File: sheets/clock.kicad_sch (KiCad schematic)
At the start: 27 parts, among them U33 74HC04, U39 CX23065A, U8 74HC04, X1 24.167829MHz, X2 3.579545MHz

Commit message: Merged in schematics from stable with footprints
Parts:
- D3: footprint (none) -> Diode_THT:D_A-405_P10.16mm_Horizontal
- TP1, TP2: footprint (none) -> TestPoint:TestPoint_Pad_D4.0mm
- U33, U8: footprint (none) -> Package_DIP:DIP-14_W7.62mm
- X1, X2: footprint (none) -> Crystal:Crystal_HC33-U_Horizontal

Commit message: FIX 74AS04 and 74HC04
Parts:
- removed unit 4 of U8
- added unit 5 of U8
- renumbered U33 to U8, U8 to U80
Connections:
- net DIVI: now also U8.10; no longer U8.12
- net at C55.2, R72.1, TC1.1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: now also U8.13
- net at C52.2, C65.1, R72.2: now also U8.12, U8.11; no longer U8.13
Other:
- moved on the sheet: U8F

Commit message: Forgot Footprint on U8
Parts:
- U8: footprint (none) -> Package_DIP:DIP-14_W7.62mm
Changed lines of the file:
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@@
     (property "Reference" "U8" (id 0) (at 311.912 110.49 0))
     (property "Value" "74HC04" (id 1) (at 313.436 119.888 0))
-    (property "Footprint" "" (id 2) (at 312.166 115.316 0)
+    (property "Footprint" "Package_DIP:DIP-14_W7.62mm" (id 2) (at 312.166 115.316 0)
       (effects (font (size 1.27 1.27)) hide)
     )

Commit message: Sync footprints from Nightly Build
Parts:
- U39: footprint Package_DIP:DIP-28_W15.24mm -> 1_NeoGeoLibrary:CX23065A
- X1, X2: footprint Crystal:Crystal_HC33-U_Horizontal -> 1_NeoGeoLibrary:Crystal
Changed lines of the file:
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@@
     (property "Reference" "X1" (id 0) (at 139.7 97.155 0))
     (property "Value" "24.167829MHz" (id 1) (at 146.685 105.41 0))
-    (property "Footprint" "Crystal:Crystal_HC33-U_Horizontal" (id 2) (at 139.7 100.965 0)
+    (property "Footprint" "1_NeoGeoLibrary:Crystal" (id 2) (at 139.7 100.965 0)
       (effects (font (size 1.27 1.27)) hide)
     )
@@
     (property "Reference" "U39" (id 0) (at 189.23 147.955 0))
     (property "Value" "CX23065A" (id 1) (at 194.945 166.37 0))
-    (property "Footprint" "Package_DIP:DIP-28_W15.24mm" (id 2) (at 194.945 174.625 0)
+    (property "Footprint" "1_NeoGeoLibrary:CX23065A" (id 2) (at 194.945 174.625 0)
       (effects (font (size 1.27 1.27)) hide)
     )
@@
     (property "Reference" "X2" (id 0) (at 261.366 81.661 0))
     (property "Value" "3.579545MHz" (id 1) (at 266.446 89.281 0))
-    (property "Footprint" "Crystal:Crystal_HC33-U_Horizontal" (id 2) (at 261.366 85.471 0)
+    (property "Footprint" "1_NeoGeoLibrary:Crystal" (id 2) (at 261.366 85.471 0)
       (effects (font (size 1.27 1.27)) hide)
     )

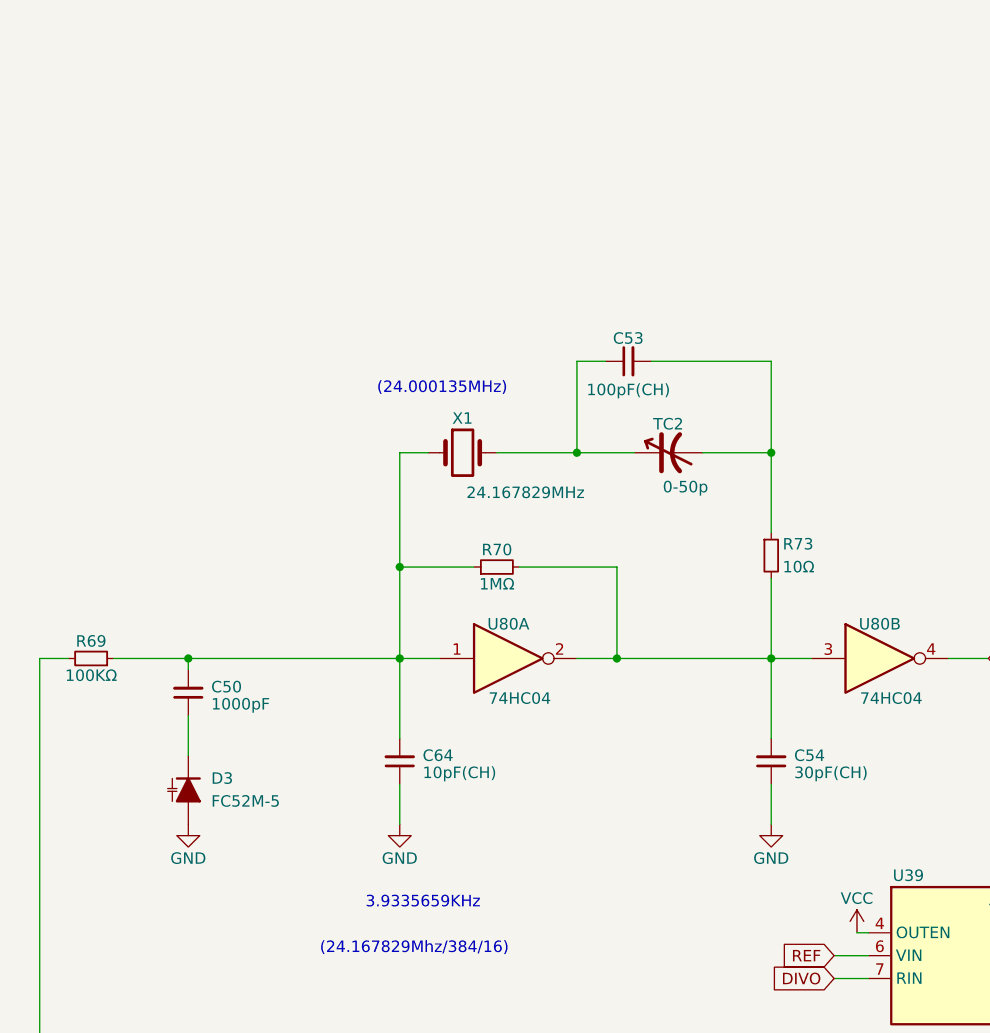
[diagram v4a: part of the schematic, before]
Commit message: Redo Video Clock Signal (1)
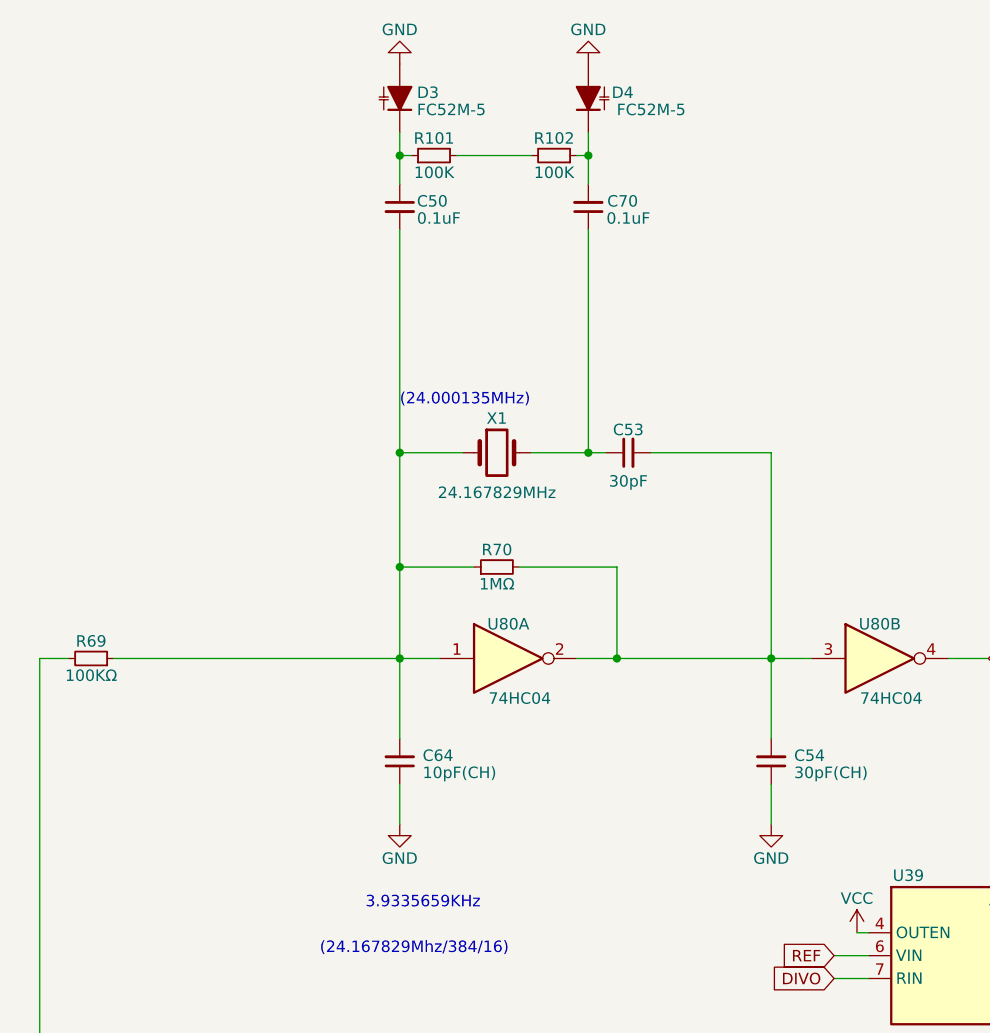
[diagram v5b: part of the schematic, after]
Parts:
- removed R73: 10Ω, 1_NeoGeoLibrary:Resistor1-5mm, symbol Device:R_Small
- removed TC2: 0-50p, Resistor_THT:R_Axial_DIN0204_L3.6mm_D1.6mm_P5.08mm_Vertical, symbol Device:C_Variable
- added C70: 0.1uF, 1_NeoGeoLibrary:CAP1-5mm, symbol Device:C_Small
- added D4: FC52M-5, Package_TO_SOT_THT:SOD-70_P2.54mm, symbol Device:D_Capacitance_Filled
- added R101, R102: 100K, 1_NeoGeoLibrary:Resistor1-5mm, symbol Device:R_Small
- C50: value 1000pF -> 0.1uF
- C53: value 100pF(CH) -> 30pF
- D3: footprint Diode_THT:D_A-405_P10.16mm_Horizontal -> Package_TO_SOT_THT:SOD-70_P2.54mm
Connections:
- net GND: now also D4.2 (A)
- net at C53.2: now also C54.2, R70.2, U80.2, U80.3
- net at C53.1, X1.2: now also C70.1
- net at C50.1, D3.1 (K): now also R101.1
- new net: R101.2, R102.2
- new net: C70.2, D4.1 (K), R102.1
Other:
- moved on the sheet: C50, C53, D3, X1

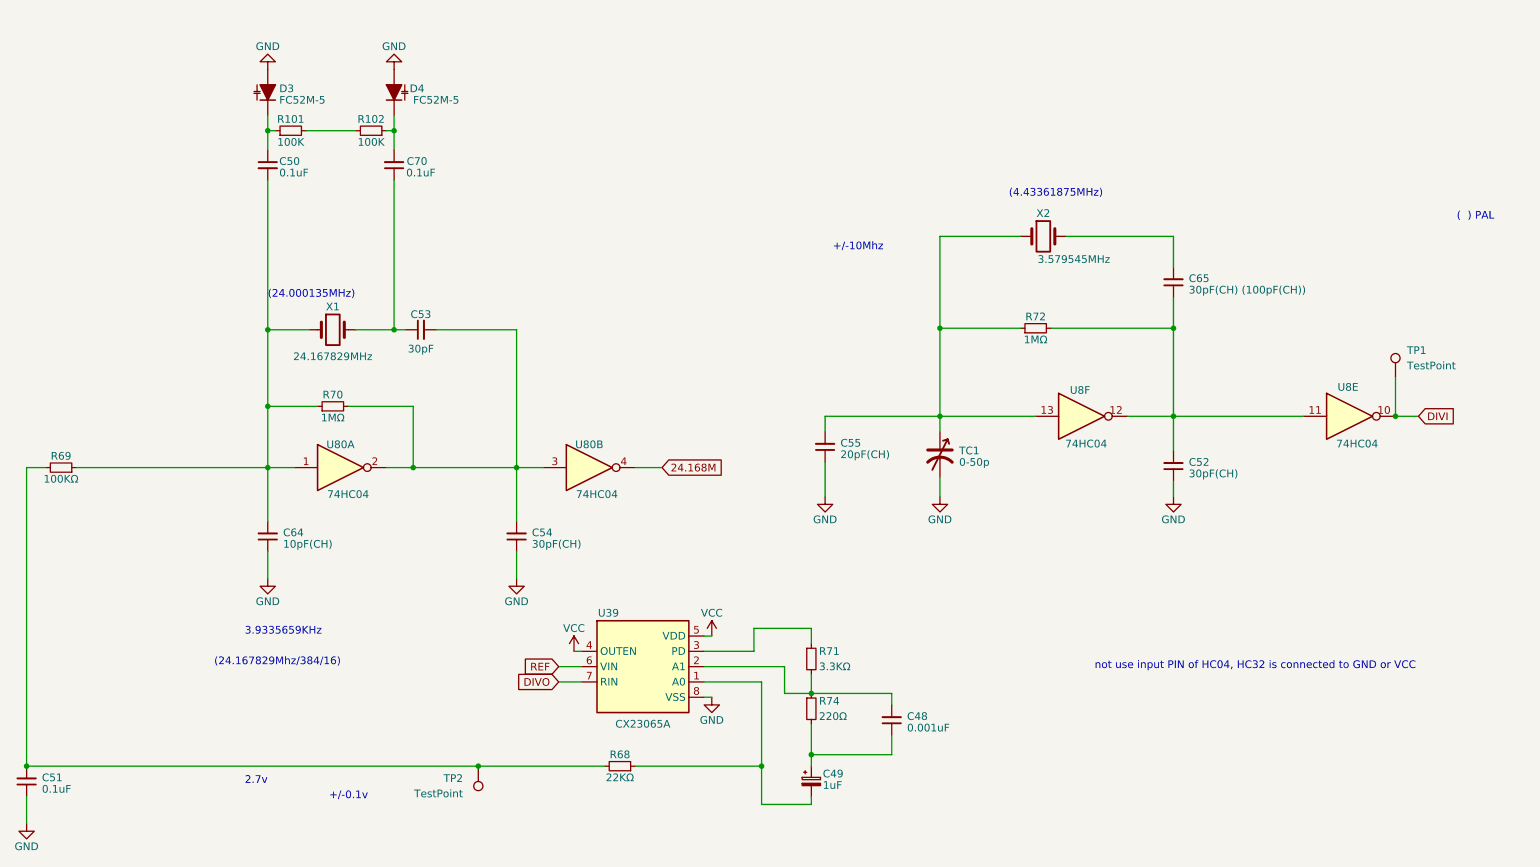
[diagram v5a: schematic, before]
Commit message: Redo Video Clock Signal (2)
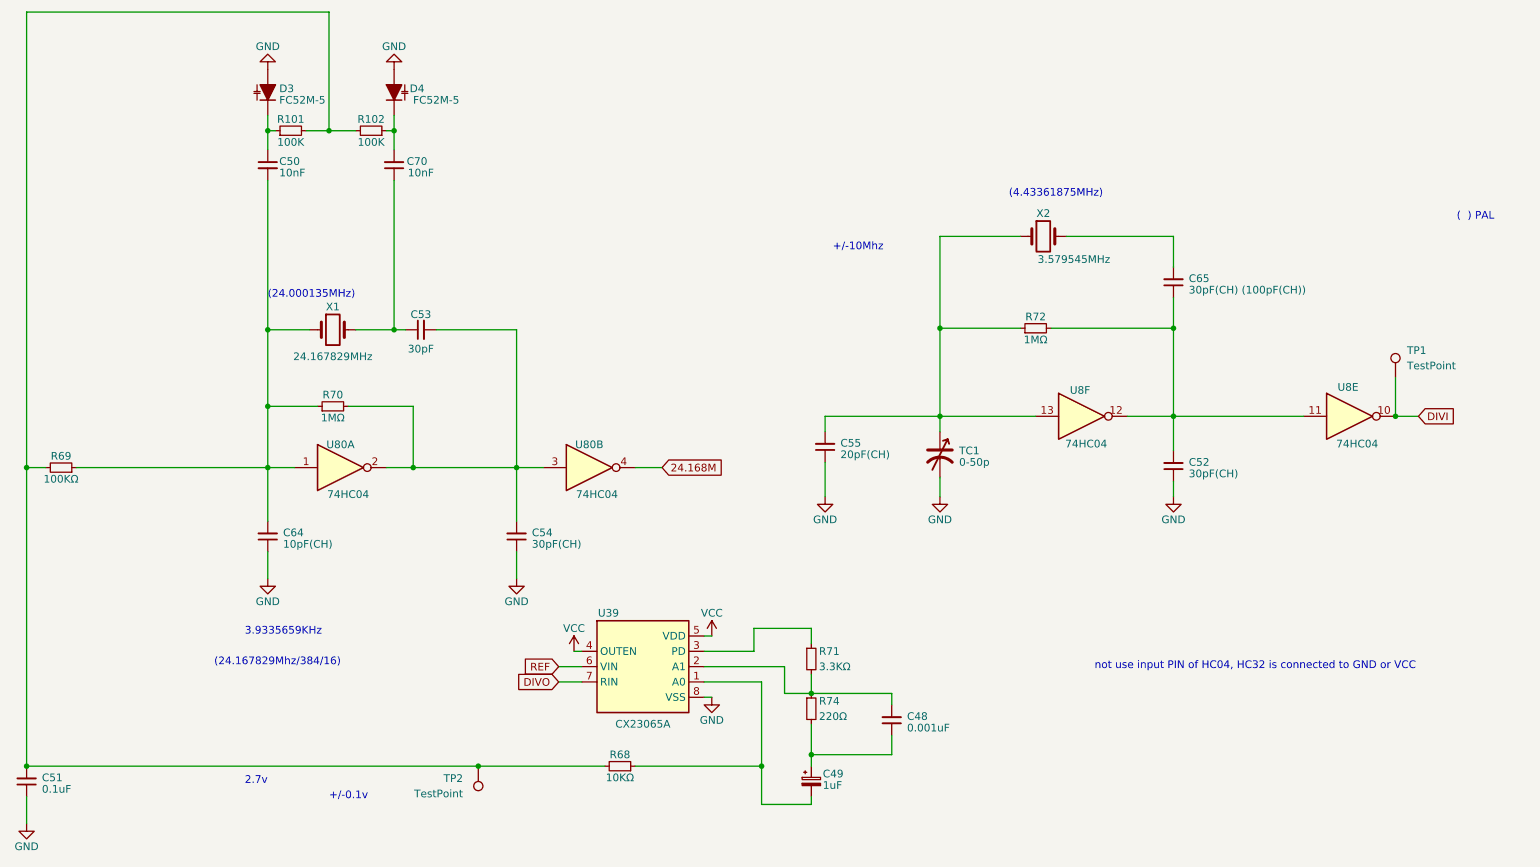
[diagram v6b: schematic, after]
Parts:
- C50, C70: value 0.1uF -> 10nF; footprint 1_NeoGeoLibrary:CAP1-5mm -> 1_NeoGeoLibrary:CAP3-5mm
- R68: value 22KΩ -> 10KΩ
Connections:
- net at C51.2, R68.2, R69.2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: now also R101.2, R102.2
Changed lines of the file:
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@@
   (junction (at 319.786 115.316) (diameter 0) (color 0 0 0 0)
   )
+  (junction (at 142.875 67.945) (diameter 0) (color 0 0 0 0)
+  )
+  (junction (at 92.71 123.825) (diameter 0) (color 0 0 0 0)
+  )
   (junction (at 132.715 100.965) (diameter 0) (color 0 0 0 0)
   )
@@
     (stroke (width 0) (type default) (color 0 0 0 0))
   )
+  (wire (pts (xy 92.71 48.26) (xy 92.71 123.825))
+    (stroke (width 0) (type default) (color 0 0 0 0))
+  )
   (wire (pts (xy 132.715 65.405) (xy 132.715 67.945))
     (stroke (width 0) (type default) (color 0 0 0 0))
@@
     (stroke (width 0) (type default) (color 0 0 0 0))
   )
-  (wire (pts (xy 139.065 67.945) (xy 147.32 67.945))
+  (wire (pts (xy 139.065 67.945) (xy 142.875 67.945))
     (stroke (width 0) (type default) (color 0 0 0 0))
   )
@@
     (stroke (width 0) (type default) (color 0 0 0 0))
   )
+  (wire (pts (xy 142.875 48.26) (xy 142.875 67.945))
+    (stroke (width 0) (type default) (color 0 0 0 0))
+  )
   (wire (pts (xy 205.105 159.385) (xy 214.63 159.385))
     (stroke (width 0) (type default) (color 0 0 0 0))
@@
     (stroke (width 0) (type default) (color 0 0 0 0))
   )
+  (wire (pts (xy 142.875 48.26) (xy 92.71 48.26))
+    (stroke (width 0) (type default) (color 0 0 0 0))
+  )
   (wire (pts (xy 236.22 161.29) (xy 236.22 163.195))
     (stroke (width 0) (type default) (color 0 0 0 0))
@@
   )
   (wire (pts (xy 180.975 156.845) (xy 184.785 156.845))
+    (stroke (width 0) (type default) (color 0 0 0 0))
+  )
+  (wire (pts (xy 142.875 67.945) (xy 147.32 67.945))
     (stroke (width 0) (type default) (color 0 0 0 0))
   )
@@
     (in_bom yes) (on_board yes)
     (property "Reference" "R68" (id 0) (at 191.135 171.45 90))
-    (property "Value" "22KΩ" (id 1) (at 191.135 175.26 90))
+    (property "Value" "10KΩ" (id 1) (at 191.135 175.26 90))
     (property "Footprint" "1_NeoGeoLibrary:Resistor1-5mm" (id 2) (at 191.135 173.355 0)
       (effects (font (size 1.27 1.27)) hide)
@@
     (in_bom yes) (on_board yes)
     (property "Reference" "C70" (id 0) (at 157.48 73.025 0))
-    (property "Value" "0.1uF" (id 1) (at 158.115 74.93 0))
-    (property "Footprint" "1_NeoGeoLibrary:CAP1-5mm" (id 2) (at 153.67 73.66 0)
+    (property "Value" "10nF" (id 1) (at 158.115 74.93 0))
+    (property "Footprint" "1_NeoGeoLibrary:CAP3-5mm" (id 2) (at 153.67 73.66 0)
       (effects (font (size 1.27 1.27)) hide)
     )
@@
       (effects (font (size 1.27 1.27)) (justify right))
     )
-    (property "Value" "0.1uF" (id 1) (at 134.62 74.93 0)
-      (effects (font (size 1.27 1.27)) (justify right))
-    )
-    (property "Footprint" "1_NeoGeoLibrary:CAP1-5mm" (id 2) (at 132.715 73.66 0)
-      (effects (font (size 1.27 1.27)) hide)
-    )
+    (property "Value" "10nF" (id 1) (at 134.62 74.93 0)
+      (effects (font (size 1.27 1.27)) (justify right))
+    )
+    (property "Footprint" "1_NeoGeoLibrary:CAP3-5mm" (id 2) (at 132.715 73.66 0)
+      (effects (font (size 1.27 1.27)) hide)
+    )

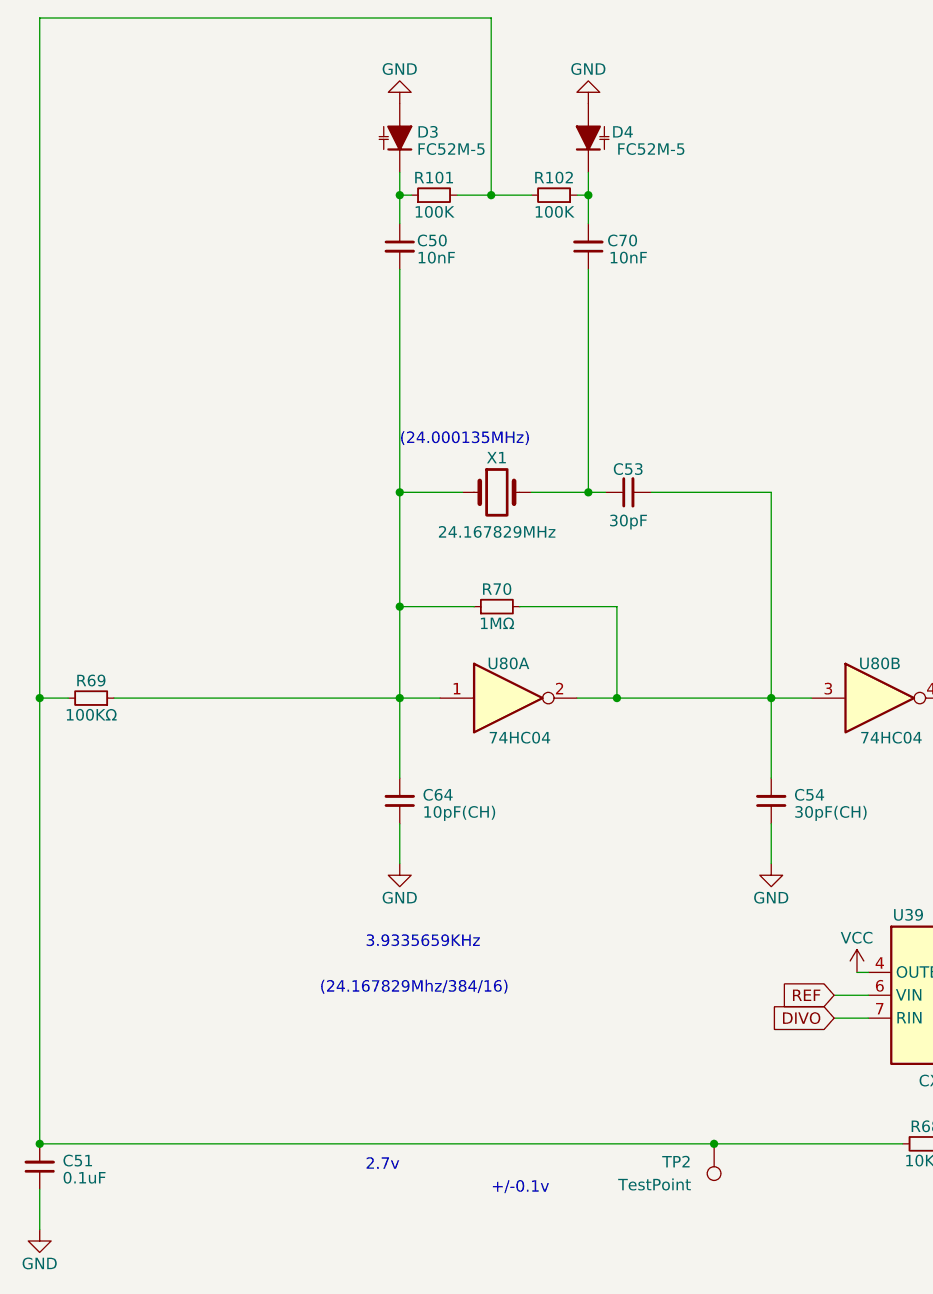
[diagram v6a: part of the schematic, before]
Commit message: Redo Video Clock Signal (3)
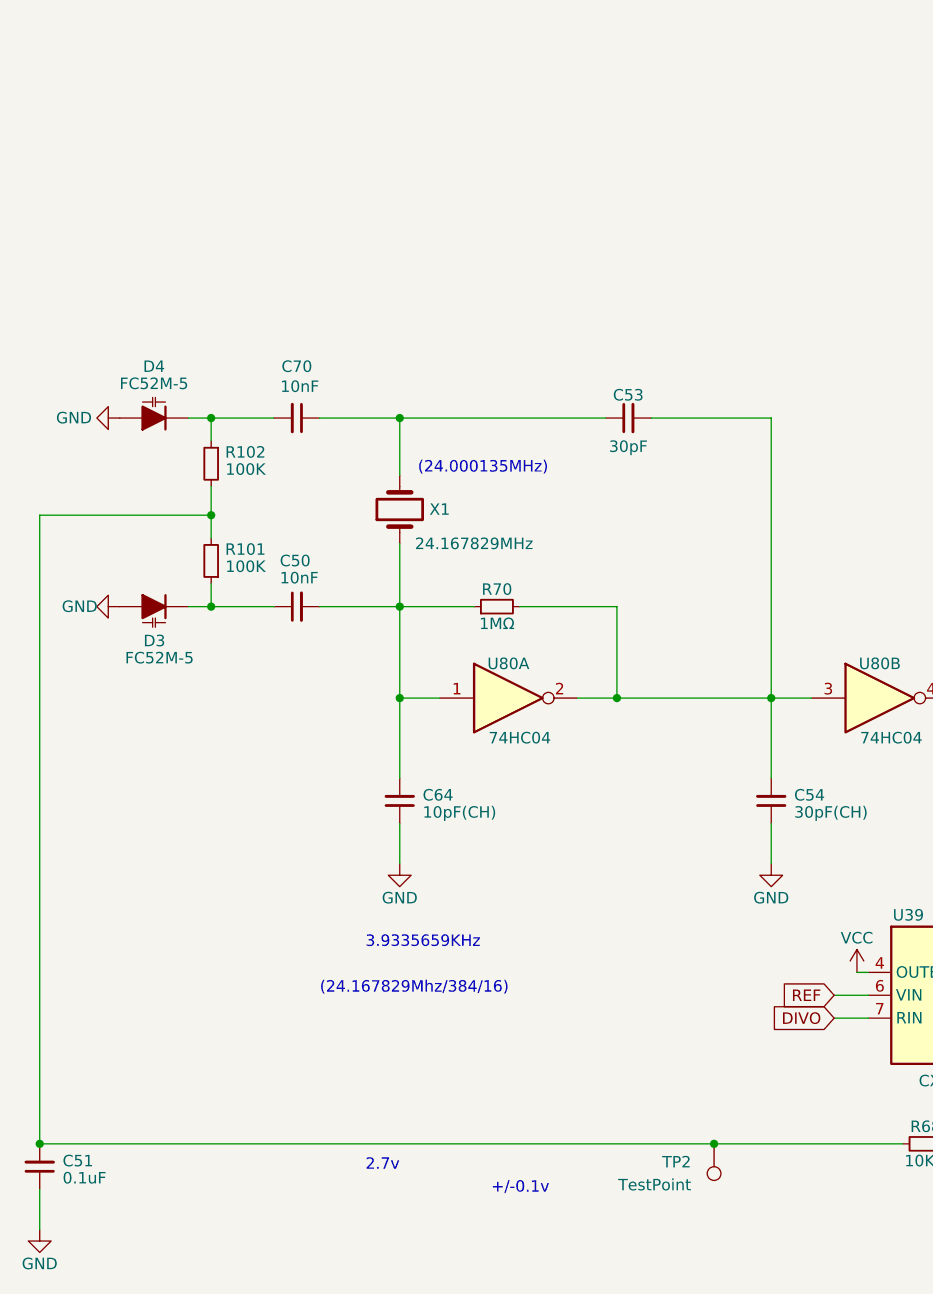
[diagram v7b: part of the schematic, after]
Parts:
- removed R69: 100KΩ, 1_NeoGeoLibrary:Resistor1-5mm, symbol Device:R_Small
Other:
- moved on the sheet: C50, C53, C70, D3, D4, R101, R102, X1
